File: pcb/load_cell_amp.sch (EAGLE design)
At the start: 6 parts, among them IC2 INA122P, J1 LOAD_CELL, J2 G29

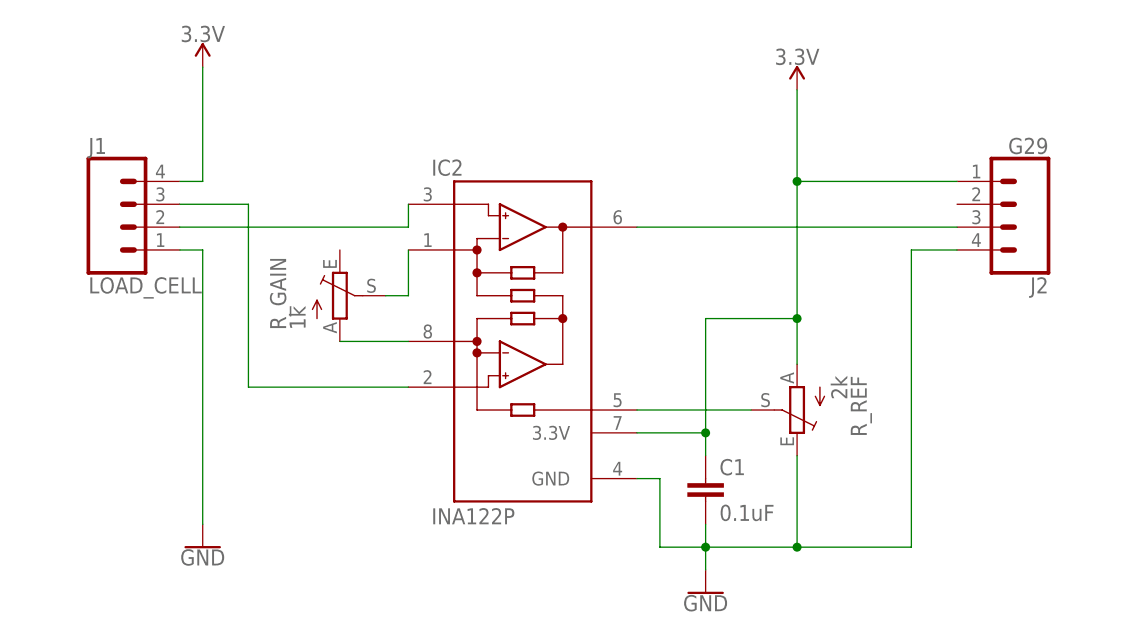
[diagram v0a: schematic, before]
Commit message: renamed IC2 to IC1
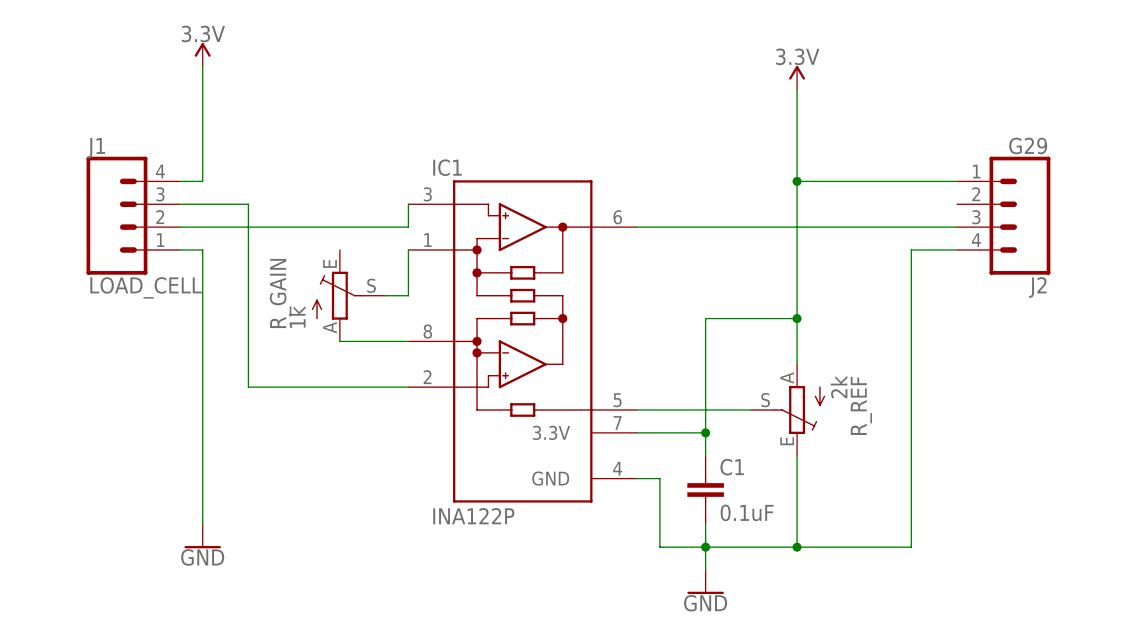
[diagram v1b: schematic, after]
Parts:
- renumbered IC2 to IC1
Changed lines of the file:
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@@
 <part name="GND2" library="SparkFun-PowerSymbols" deviceset="GND" device=""/>
 <part name="SUPPLY2" library="SparkFun-PowerSymbols" deviceset="3.3V" device=""/>
-<part name="IC2" library="g29_load_cell" deviceset="INA122" device="P" package3d_urn="urn:adsk.eagle:package:4906/1"/>
+<part name="IC1" library="g29_load_cell" deviceset="INA122" device="P" package3d_urn="urn:adsk.eagle:package:4906/1"/>
 </parts>
 <sheets>
@@
 <attribute name="VALUE" x="50.8" y="33.274" size="1.778" layer="96" align="bottom-center"/>
 </instance>
-<instance part="IC2" gate="G$1" x="20.32" y="2.54" smashed="yes">
+<instance part="IC1" gate="G$1" x="20.32" y="2.54" smashed="yes">
 <attribute name="NAME" x="10.16" y="20.955" size="1.778" layer="95" ratio="10"/>
 <attribute name="VALUE" x="10.16" y="-17.78" size="1.778" layer="96" ratio="10"/>
@@
 <pinref part="R_GAIN" gate="1" pin="A"/>
 <wire x1="7.62" y1="2.54" x2="0" y2="2.54" width="0.1524" layer="91"/>
-<pinref part="IC2" gate="G$1" pin="RG@1"/>
+<pinref part="IC1" gate="G$1" pin="RG@1"/>
 </segment>
 </net>
@@
 <wire x1="7.62" y1="12.7" x2="7.62" y2="7.62" width="0.1524" layer="91"/>
 <wire x1="7.62" y1="7.62" x2="5.08" y2="7.62" width="0.1524" layer="91"/>
-<pinref part="IC2" gate="G$1" pin="RG"/>
+<pinref part="IC1" gate="G$1" pin="RG"/>
 </segment>
 </net>
@@
 <wire x1="63.5" y1="-20.32" x2="50.8" y2="-20.32" width="0.1524" layer="91"/>
 <junction x="50.8" y="-20.32"/>
-<pinref part="IC2" gate="G$1" pin="GND"/>
+<pinref part="IC1" gate="G$1" pin="GND"/>
 </segment>
 </net>
@@
 <junction x="40.64" y="-7.62"/>
 <junction x="50.8" y="5.08"/>
-<pinref part="IC2" gate="G$1" pin="3.3V"/>
+<pinref part="IC1" gate="G$1" pin="3.3V"/>
 </segment>
 </net>
@@
 <pinref part="R_REF" gate="1" pin="S"/>
 <wire x1="33.02" y1="-5.08" x2="45.72" y2="-5.08" width="0.1524" layer="91"/>
-<pinref part="IC2" gate="G$1" pin="REF"/>
+<pinref part="IC1" gate="G$1" pin="REF"/>
 </segment>
 </net>
@@
 <pinref part="J2" gate="J1" pin="3"/>
 <wire x1="33.02" y1="15.24" x2="68.58" y2="15.24" width="0.1524" layer="91"/>
-<pinref part="IC2" gate="G$1" pin="OUT"/>
+<pinref part="IC1" gate="G$1" pin="OUT"/>
 </segment>
 </net>
@@
 <wire x1="-17.78" y1="15.24" x2="7.62" y2="15.24" width="0.1524" layer="91"/>
 <wire x1="7.62" y1="15.24" x2="7.62" y2="17.78" width="0.1524" layer="91"/>
-<pinref part="IC2" gate="G$1" pin="+IN"/>
+<pinref part="IC1" gate="G$1" pin="+IN"/>
 </segment>
 </net>
@@
 <wire x1="-10.16" y1="17.78" x2="-10.16" y2="-2.54" width="0.1524" layer="91"/>
 <wire x1="-10.16" y1="-2.54" x2="7.62" y2="-2.54" width="0.1524" layer="91"/>
-<pinref part="IC2" gate="G$1" pin="-IN"/>
+<pinref part="IC1" gate="G$1" pin="-IN"/>
 </segment>
 </net>

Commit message: updated schematic to support single cell
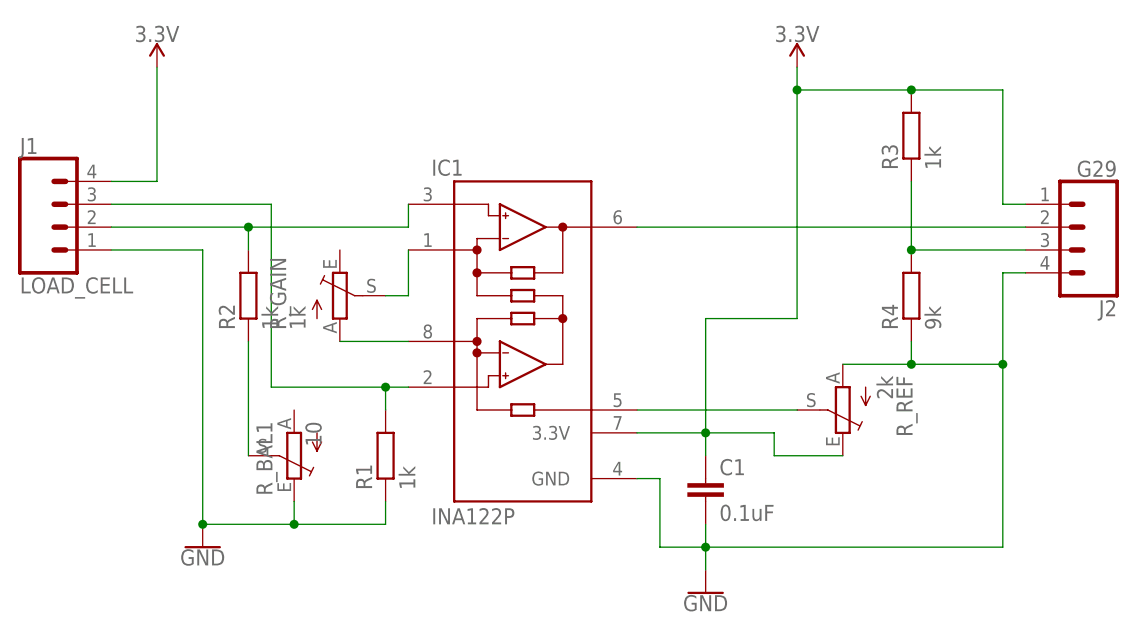
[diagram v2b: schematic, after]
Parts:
- added R1, R2, R3: 1k, rcl:R-EU_0207/10
- added R4: 9k, rcl:R-EU_0207/10
- added R_BAL1: 10, pot:TRIM_EU-RJ9W
- J1, J2: device SparkFun-Connectors:CONN_04SCREW -> con-amp-quick:M04
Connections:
- removed net N$7: IC1.OUT, J2.3
- new net CLUTCH: IC1.OUT, J2.2
- new net N$5: R2.1, R_BAL1.S
- new net N$9: J2.3, R3.1, R4.2
- net 3.3V: now also R3.2, R_REF.E; no longer R_REF.A
- net GND: now also R1.1, R4.1, R_BAL1.E, R_REF.A; no longer R_REF.E
- net N$3: now also R2.2
- net N$4: now also R1.2
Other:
- moved on the sheet: R_REF
